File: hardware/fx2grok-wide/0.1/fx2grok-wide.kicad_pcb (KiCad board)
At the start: 2 copper layers, 43 parts, among them IC1 CY7C68013A-56, J1 Conn_02x05_Odd_Even, J2 Conn_02x05_Odd_Even, P1 pkl_USB_OTG, U1 3.3V, U2 USBLC6-2, U3 DSILC6-4, U4 DSILC6-4, U5 pkl_24LC00, U6 DSILC6-4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

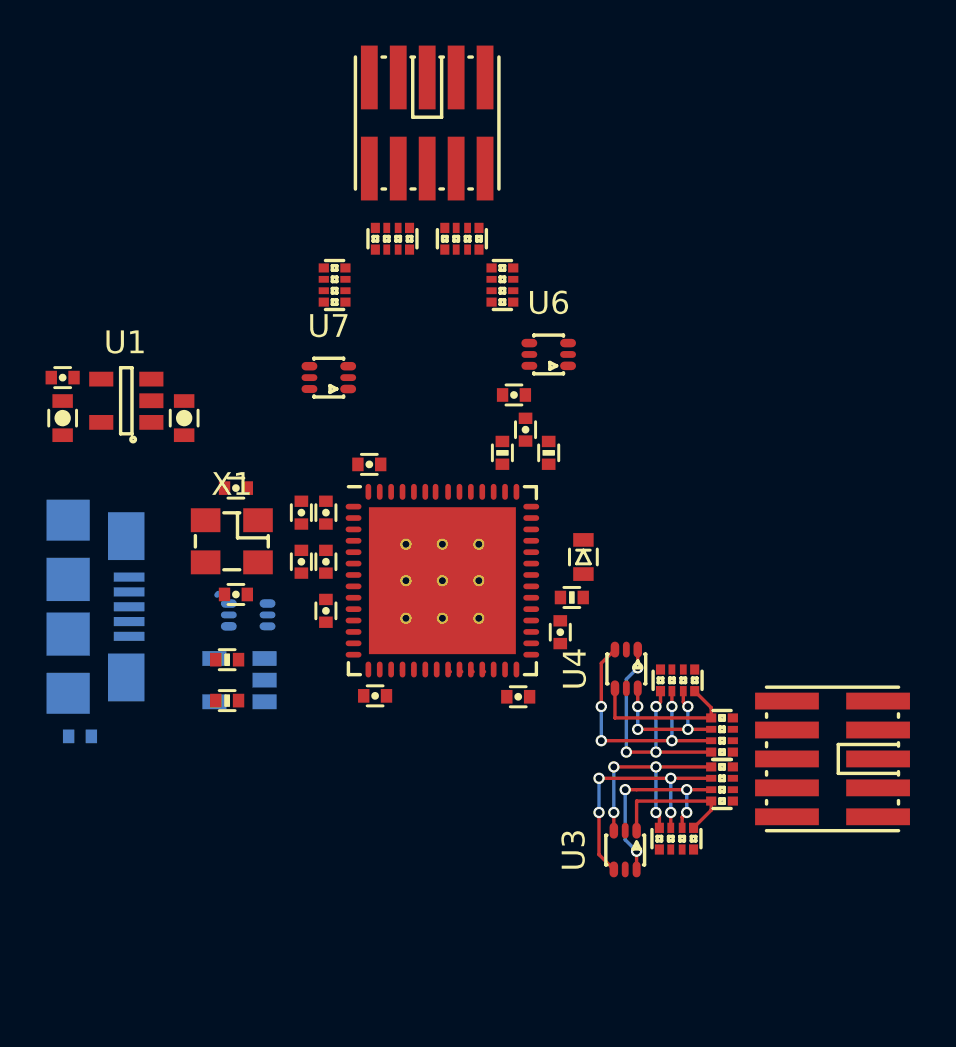
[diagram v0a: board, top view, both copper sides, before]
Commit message: Switch to a different footprint for the FX2, and make the input connectors SMD pads on both sides of the PCB(Can stick a 2x5 through-hole header over the side of the PCB and solder it on). Made a bunch of progress on laying out the PCB, currently ~1.5sqin. Not particularly happy with how the inputs come out on opposite ends of the thing, but that's how the chip wants them to be laid out.
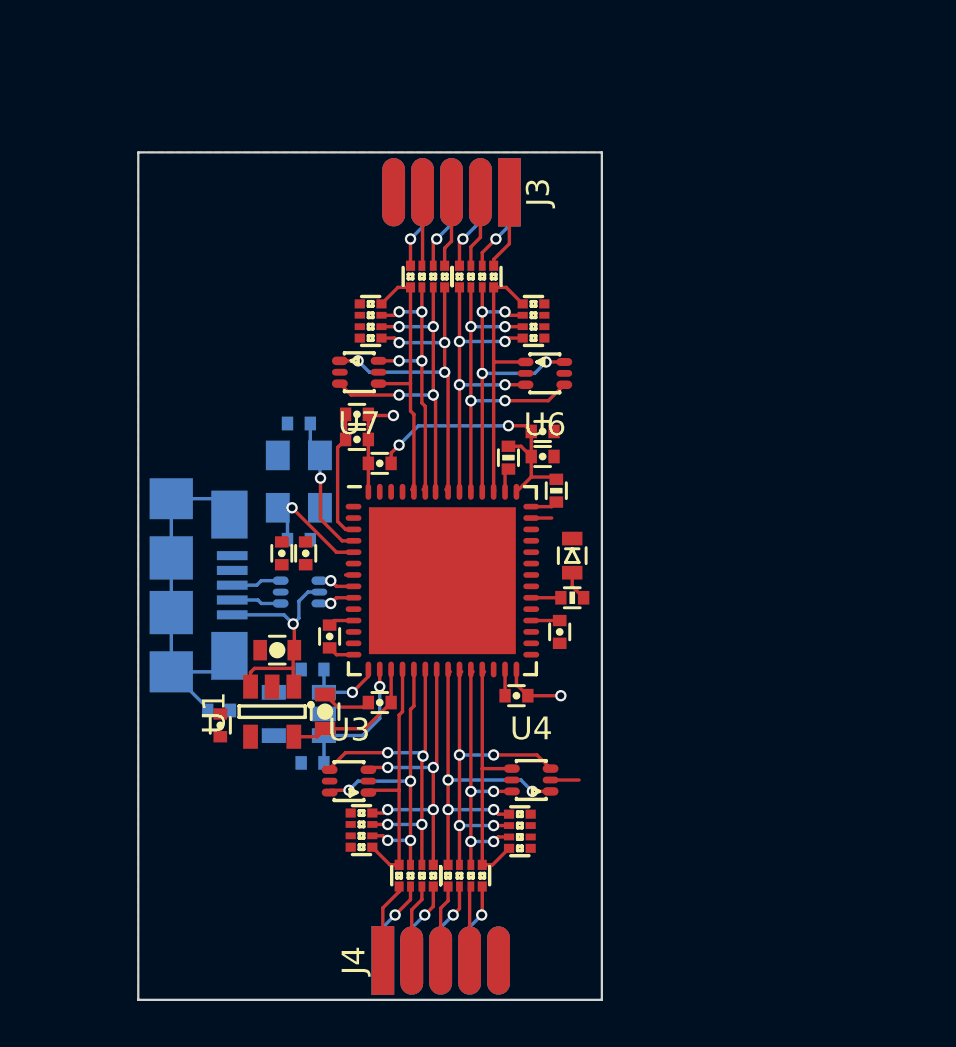
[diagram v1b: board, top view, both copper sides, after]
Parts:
- removed J1, J2: Conn_02x05_Odd_Even, pkl_samtec:FTSH-105-XX-X-DV
- added J3: CONN_01X05, izzy:Pin_Header_Angled_1x05_Pitch1.27mm_SMD, F.Cu at (161.8, 51.3)
- added J4: CONN_01X05, izzy:Pin_Header_Angled_1x05_Pitch1.27mm_SMD, F.Cu at (161.4, 85.0)
- added J5: CONN_01X05, izzy:Pin_Header_Angled_1x05_Pitch1.27mm_SMD, B.Cu at (161.4, 85.0)
- added J6: CONN_01X05, izzy:Pin_Header_Angled_1x05_Pitch1.27mm_SMD, B.Cu at (161.8, 51.3)
- C15, C16, R2, R3, X1: moved to B.Cu
- IC1: footprint pkl_housings_dfn_qfn:QFN-56-1EP_8x8mm_Pitch0.5mm -> izzy:QFN-56-1EP_8x8mm_Pitch0.5mm-novias
- moved C13 17.3 mm to (156.3, 74.1)
- moved C12 16.8 mm to (151.7, 74.7), turned to 90 degrees
- moved U1 15.1 mm to (154.0, 74.1), turned to 90 degrees
- moved R6 14.0 mm to (160.3, 81.3), turned to 0 degrees
- moved R8 13.8 mm to (157.9, 79.3), turned to 90 degrees
- moved R7 12.9 mm to (162.4, 81.3), turned to 0 degrees
- moved U3 12.5 mm to (157.3, 77.2), turned to 0 degrees
- moved C11 11.0 mm to (154.2, 71.4), turned to 180 degrees
- moved R9 9.58 mm to (164.8, 79.3), turned to 270 degrees
- moved U4 6.42 mm to (165.3, 77.1), turned to 0 degrees
- moved R10 6.21 mm to (151.7, 74.0)
- moved R3 4.64 mm to (155.8, 76.3)
- moved P1 4.63 mm to (149.6, 68.5)
- moved C7 4.52 mm to (157.7, 61.0), turned to 0 degrees
- moved C9 4.04 mm to (157.7, 62.1), turned to 0 degrees
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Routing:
- net +3V3: track 0.00 -> 28.4 mm, vias 0 -> 2
- net /PD4: track 0.00 -> 16.9 mm, vias 0 -> 4
- net /PD5: track 0.00 -> 15.9 mm, vias 0 -> 4
- net /PD2: track 0.00 -> 15.8 mm, vias 0 -> 4
- net /shield: track 0.00 -> 15.6 mm
- net /PD3: track 0.00 -> 14.8 mm, vias 0 -> 4
- net /PD1: track 0.00 -> 14.7 mm, vias 0 -> 4
- net GND: track 0.00 -> 13.9 mm, vias 0 -> 2
- net /PD6: track 0.00 -> 13.0 mm, vias 0 -> 4
- net /PD7: track 0.00 -> 12.2 mm
- net /PD0: track 0.00 -> 12.0 mm
- net +5V: track 0.00 -> 10.4 mm, vias 0 -> 1
- net /XTALOUT: track 0.00 -> 6.23 mm, vias 0 -> 1
- net /SDA: track 0.00 -> 6.11 mm, vias 0 -> 1
- net /XTALIN: track 0.00 -> 5.71 mm, vias 0 -> 1
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- added copper zone on B.Cu, net GND
- added copper zone on F.Cu, net GND
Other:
- board outline added: 20.3 x 37.2 mm

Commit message: Switch back to the old FX2 footprint, add the center pad of the QFN to the schematic symbol, and connect it to ground as recommended by Cypress. And connect a few more traces.
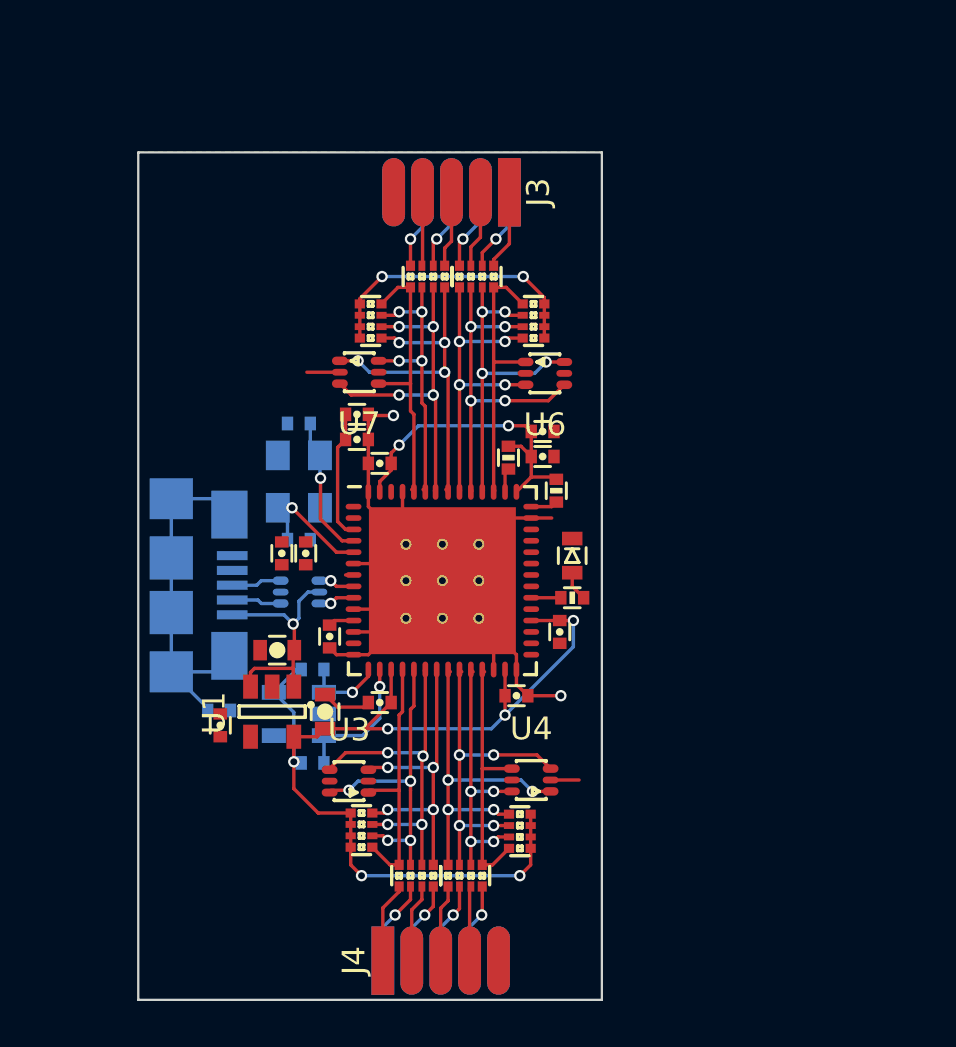
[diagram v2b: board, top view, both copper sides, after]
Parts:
- IC1: value CY7C68013A-56 -> CY7C68013A-56-QFN; footprint izzy:QFN-56-1EP_8x8mm_Pitch0.5mm-novias -> pkl_housings_dfn_qfn:QFN-56-1EP_8x8mm_Pitch0.5mm
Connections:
- IC1 pad 57: (no net) -> GND
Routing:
- net +3V3: track 28.4 -> 78.8 mm, vias 2 -> 10
- net GND: track 13.9 -> 30.5 mm
